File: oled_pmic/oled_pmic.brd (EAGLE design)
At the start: 16.5 x 16 mm, 11 parts, among them J1 I_sense, J2 VCC, J4 GND, Q1 N-CHANNEL-MOSFETSOT23-3, U1 AL5801W6-7

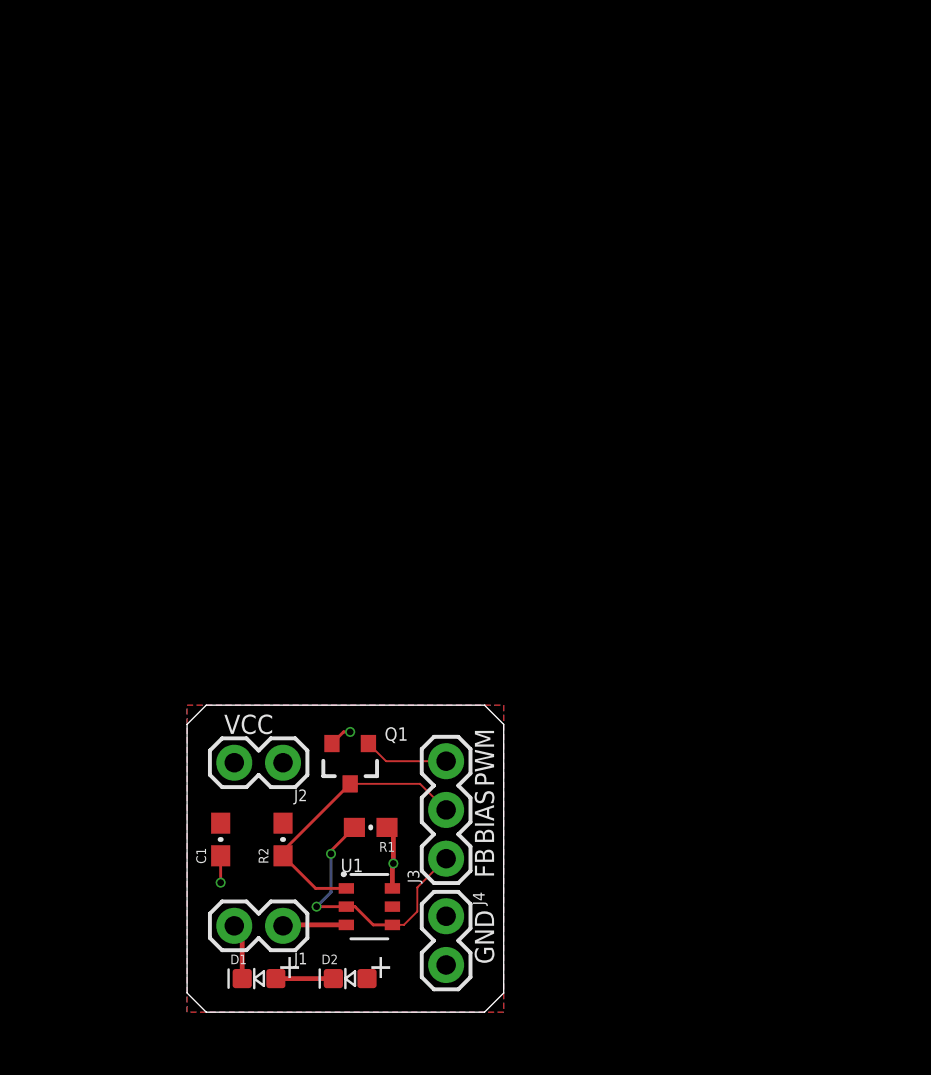
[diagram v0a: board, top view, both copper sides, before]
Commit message: start oled pmic module
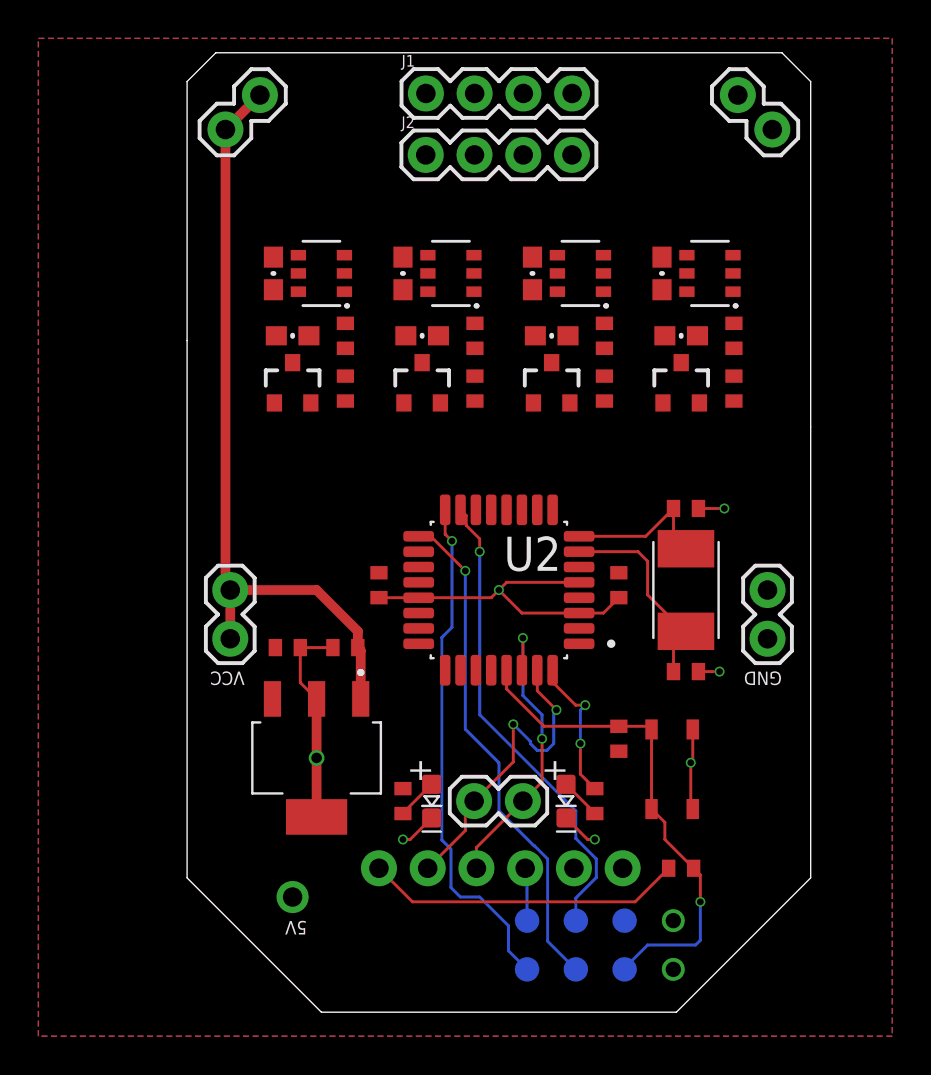
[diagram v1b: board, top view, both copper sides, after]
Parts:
- removed C1: 0.1uF, scono:0603-CAP
- removed D1, D2: (no value), scono:LED-0603
- removed J3: (no value), scono:1X03
- removed J4: GND, scono:1X02
- added C2, C3, C4, C5, C8: 100nF, scono:0402-CAP
- added C6, C7: 18pF, scono:0402-CAP
- added D3: (no value), scono:LED-0603
- added D4: RED, scono:LED-0603
- added J10, J6: GND, scono:1X02
- added J12: BURNIN, scono:BURNIN
- added J5, J9: VCC, scono:1X02
- added J7: UART, scono:1X02
- added J8: FTDI, scono:1X06_NO_SILK
- added Q2, Q3, Q4: N-CHANNEL-MOSFETSOT23-3, scono:SOT23-3
- added R10, R11, R14, R15, R18, R19, R6, R7: 100k, scono:R0402
- added R12, R16, R8: 1.6R, scono:0603-RES
- added R13, R17, R9: 52.5k, scono:0603-RES
- added R3: 10k, scono:R0402
- added R4, R5: 500R, scono:R0402
- added SW1: BTN-PTS810, scono:BTN_PTS810
- added TP1: TEST_POINTTHRU, scono:TEST_POINT
- added U2: LM340MPX-5.0230, scono:SOT230P700X180-4N
- added U3: ATMEGA328P-AUR, scono:QFP80P900X900X120-32N
- added U4, U5, U6: AL5801W6-7, scono:SOT26
- added Y1: 16MHz, scono:XTAL500X320X130N
- J1: value I_sense -> (none); device scono:1X02 -> scono:1X04
- J2: value VCC -> (none); device scono:1X02 -> scono:1X04
- moved J1 44.0 mm to (12.4, 47.9), turned to 0 degrees
- moved U1 33.1 mm to (7.00, 38.5), turned to 180 degrees
- moved J2 32.5 mm to (12.4, 44.7), turned to 0 degrees
- moved R1 29.3 mm to (4.50, 38.5), turned to 90 degrees
- moved R2 26.3 mm to (5.50, 35.2), turned to 180 degrees
- moved Q1 20.0 mm to (5.50, 32.8), turned to 0 degrees
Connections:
- removed net BIAS: J3.2, Q1.3, R2.1, U1.1
- removed net FB: J3.1, R1.2, U1.2, U1.4
- removed net N$2: D1.A, D2.C
- removed net N$3: J1.1, U1.3
- removed net N$4: D1.C, J1.2
- removed net PWM: J3.3, Q1.1
- new net 5V: C3.2, C4.2, C5.2, J12.3.3V, J8.4, R3.2, R5.1, TP1.1, U2.3, U3.18, U3.4, U3.6
- new net ADC0: R6.1, R7.2, U3.23
- new net ADC1: R10.1, R11.2, U3.24
- new net ADC2: R14.1, R15.2, U3.25
- new net ADC3: R18.1, R19.2, U3.26
- new net AREF: U3.20
- new net BIAS1: Q1.3, R2.1, U1.1
- new net BIAS2: Q2.3, R9.1, U4.1
- new net BIAS3: Q3.3, R13.1, U5.1
- new net BIAS4: Q4.3, R17.1, U6.1
- new net CAT1: J2.1, R6.2, U1.3
- new net CAT2: J2.2, R10.2, U4.3
- new net CAT3: J2.3, R14.2, U5.3
- new net CAT4: J2.4, R18.2, U6.3
- new net CTS: J8.5
- new net FB1: R1.2, U1.2, U1.4
- new net FB2: R8.2, U4.2, U4.4
- new net FB3: R12.2, U5.2, U5.4
- new net FB4: R16.2, U6.2, U6.4
- new net GPIO0: R4.2, U3.32
- new net GPIO1: U3.1
- new net GPIO2: U3.2
- new net GPIO3: U3.9
- new net GPIO4: U3.10
- new net GPIO5: U3.11
- new net GPIO6: U3.12
- new net GPIO7: U3.13
- new net MISO: J12.MISO, U3.16
- new net MOSI: J12.MOSI, U3.15
- new net N$1: D3.A, R4.1
- new net N$5: D4.A, R5.2
- new net N$6: C8.2, J8.1
- new net PWM1: Q1.1
- new net PWM2: Q2.1
- new net PWM3: Q3.1
- new net PWM4: Q4.1
- new net RST: C8.1, J12.RST, R3.1, SW1.3, SW1.4, U3.29
- new net RX: J7.1, J8.3, U3.30
- new net SCK: J12.SCK, U3.17
- new net SCL: U3.28
- new net SDA: U3.27
- new net SS: U3.14
- new net TX: J7.2, J8.2, U3.31
- new net XTAL1: C6.1, U3.7, Y1.2
- new net XTAL2: C7.1, U3.8, Y1.1
- net GND: now also C2.1, C3.1, C4.1, C5.1, C6.2, C7.2, D3.C, D4.C, J10.1, J10.2, J12.GND, J6.1, J6.2, J8.6, Q2.2, Q3.2, Q4.2, R11.1, R12.1, R15.1, R16.1, R19.1, R7.1, R8.1, SW1.1, SW1.2, U2.2, U2.4, U3.21, U3.3, U3.5, U4.6, U5.6, U6.6; no longer C1.1, J4.1, J4.2
- net VCC: now also C2.2, J1.1, J1.2, J1.3, J1.4, J5.1, J5.2, J9.1, J9.2, R13.2, R17.2, R9.2, U2.1; no longer C1.2, D2.A, J2.1, J2.2
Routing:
- net VCC: track 0.00 -> 40.3 mm
- net GND: track 5.94 -> 39.3 mm, vias 3 -> 7
- net MISO: track 0.00 -> 26.7 mm, vias 0 -> 1
- net SCK: track 0.00 -> 26.3 mm, vias 0 -> 1
- net RST: track 0.00 -> 26.2 mm, vias 0 -> 1
- net MOSI: track 0.00 -> 24.8 mm, vias 0 -> 1
- net N$6: track 0.00 -> 16.5 mm
- net TX: track 0.00 -> 16.5 mm, vias 0 -> 2
- net RX: track 0.00 -> 15.5 mm, vias 0 -> 2
- net BIAS: track 14.9 -> 0.00 mm
- net FB: track 14.3 -> 0.00 mm, vias 2 -> 0
- net XTAL1: track 0.00 -> 10.7 mm
- net XTAL2: track 0.00 -> 7.89 mm
- net GPIO0: track 0.00 -> 7.58 mm, vias 0 -> 2
- net PWM: track 4.43 -> 0.00 mm
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- added copper zone on layer 1, net 5V
- removed copper zone on layer 1, net VCC
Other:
- board size 16.5 x 16 mm -> 32.5 x 50 mm
- board text added: "5V"
- board text added: "U2"
- board text removed: "BIAS"
- board text removed: "FB"
- board text removed: "PWM"

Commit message: finish oled module
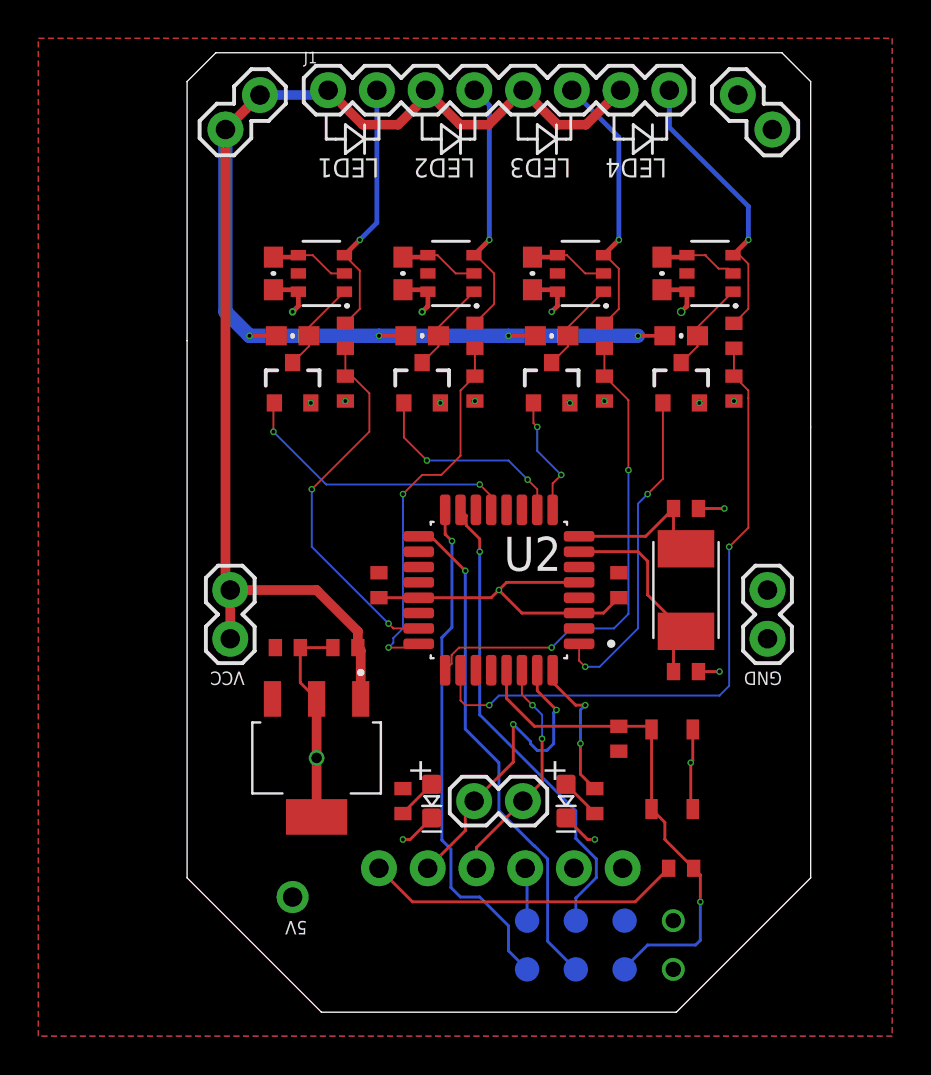
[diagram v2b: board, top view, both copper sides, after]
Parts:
- removed J2: (no value), scono:1X04
- J1: device scono:1X04 -> scono:1X08
- moved J1 5.10 mm to (7.35, 48.0)
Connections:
- removed net GPIO1: U3.1
- removed net GPIO3: U3.9
- removed net GPIO4: U3.10
- removed net GPIO7: U3.13
- net CAT1: now also J1.2; no longer J2.1
- net CAT2: now also J1.4; no longer J2.2
- net CAT3: now also J1.6; no longer J2.3
- net CAT4: now also J1.8; no longer J2.4
- net PWM1: now also U3.13
- net PWM2: now also U3.10
- net PWM3: now also U3.9
- net PWM4: now also U3.1
- net VCC: now also J1.5, J1.7; no longer J1.2, J1.4
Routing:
- net VCC: track 40.3 -> 101.0 mm, vias 0 -> 4
- net ADC3: track 0.00 -> 34.4 mm, vias 0 -> 2
- net ADC2: track 0.00 -> 25.4 mm, vias 0 -> 2
- net ADC1: track 0.00 -> 19.7 mm, vias 0 -> 2
- net ADC0: track 0.00 -> 19.6 mm, vias 0 -> 2
- net PWM4: track 0.00 -> 17.2 mm, vias 0 -> 2
- net CAT4: track 0.00 -> 15.0 mm, vias 0 -> 1
- net PWM1: track 0.00 -> 15.0 mm, vias 0 -> 2
- net CAT3: track 0.00 -> 14.2 mm, vias 0 -> 1
- net CAT2: track 0.00 -> 13.7 mm, vias 0 -> 1
- net CAT1: track 0.00 -> 13.5 mm, vias 0 -> 1
- net PWM2: track 0.00 -> 10.9 mm, vias 0 -> 2
- net GND: track 39.3 -> 49.5 mm, vias 7 -> 19
- net PWM3: track 0.00 -> 6.36 mm, vias 0 -> 2
- net BIAS4: track 0.00 -> 4.82 mm
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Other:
- board text added: "LED1"
- board text added: "LED2"
- board text added: "LED3"
- board text added: "LED4"

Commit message: update burnin drill size
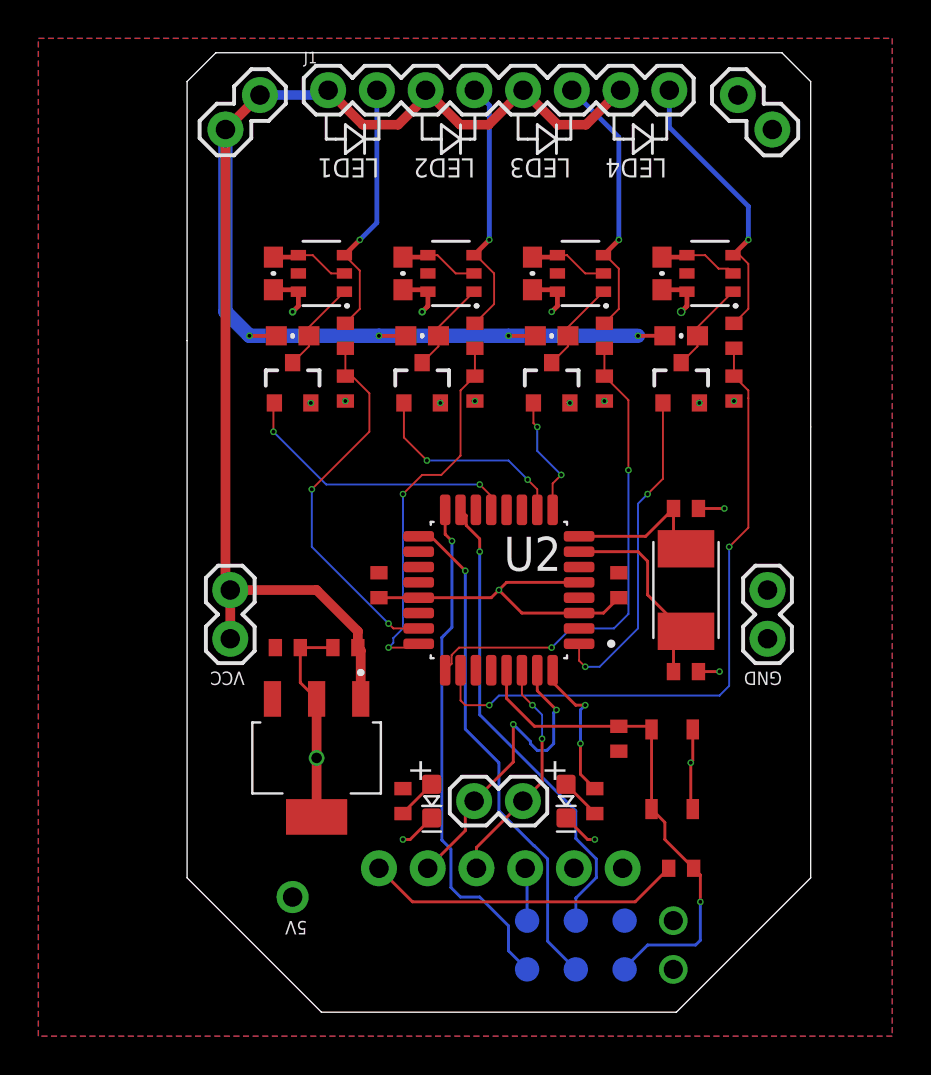
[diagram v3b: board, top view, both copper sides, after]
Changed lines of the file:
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@@
 <wire x1="25.95" y1="39.35" x2="26.05" y2="39.45" width="0.1" layer="1"/>
 <wire x1="26.05" y1="39.45" x2="27" y2="39.45" width="0.1" layer="1"/>
-<wire x1="27" y1="39.45" x2="27.05" y2="39.45" width="0.1" layer="1"/>
 <wire x1="27" y1="39.45" x2="27.7" y2="38.75" width="0.1" layer="1"/>
 <wire x1="28.2" y1="38.75" x2="28.45" y2="38.5" width="0.1" layer="1"/>

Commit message: finish boms and cams
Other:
- board text added: "Controllable OLED Module"
